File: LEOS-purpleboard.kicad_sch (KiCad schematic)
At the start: 5 parts, among them J3 Conn_01x07_Socket, J4 Conn_01x07_Socket, J5 Conn_01x06_Socket, J6 Conn_01x06_Socket, J7 Conn_01x04_Pin

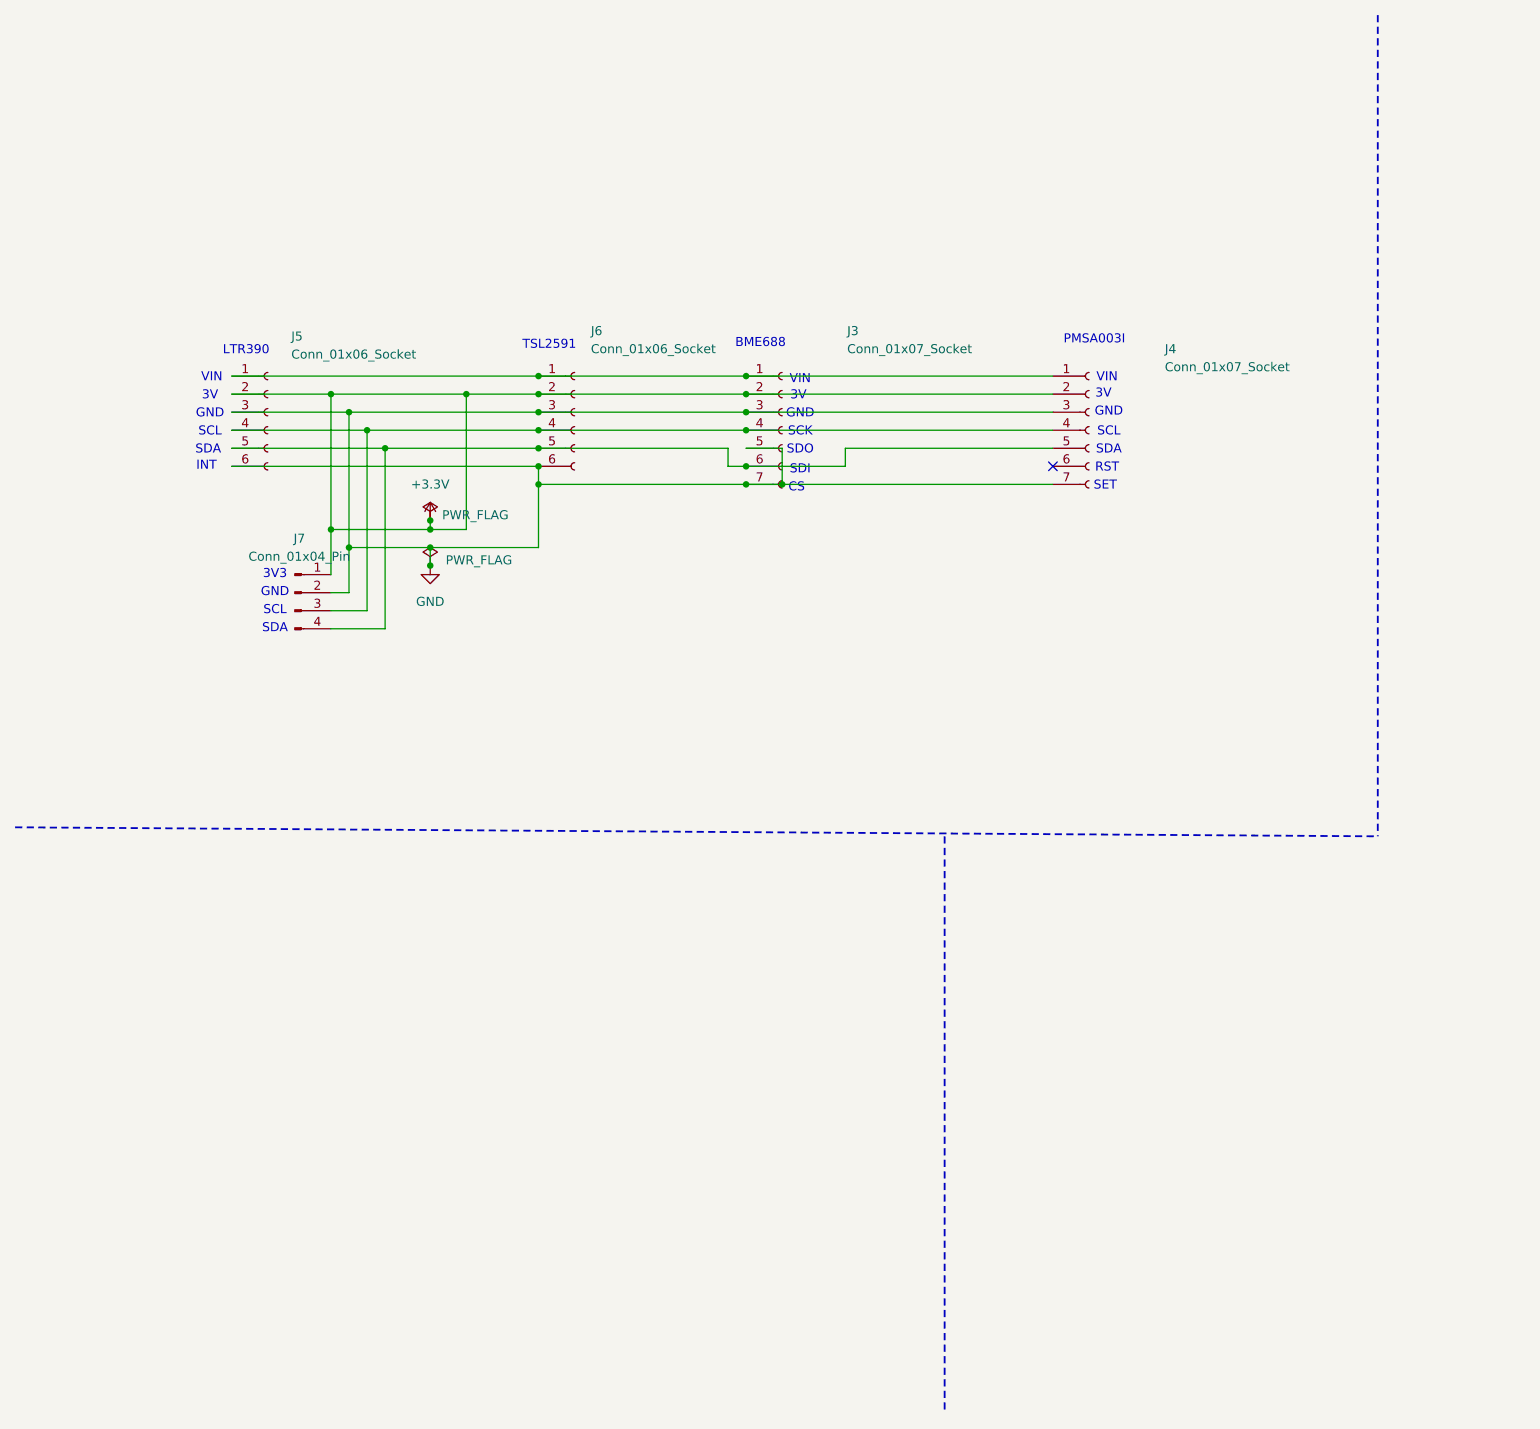
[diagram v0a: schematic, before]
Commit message: Fix flipped pinouts, update 3D model, and redesign schematic
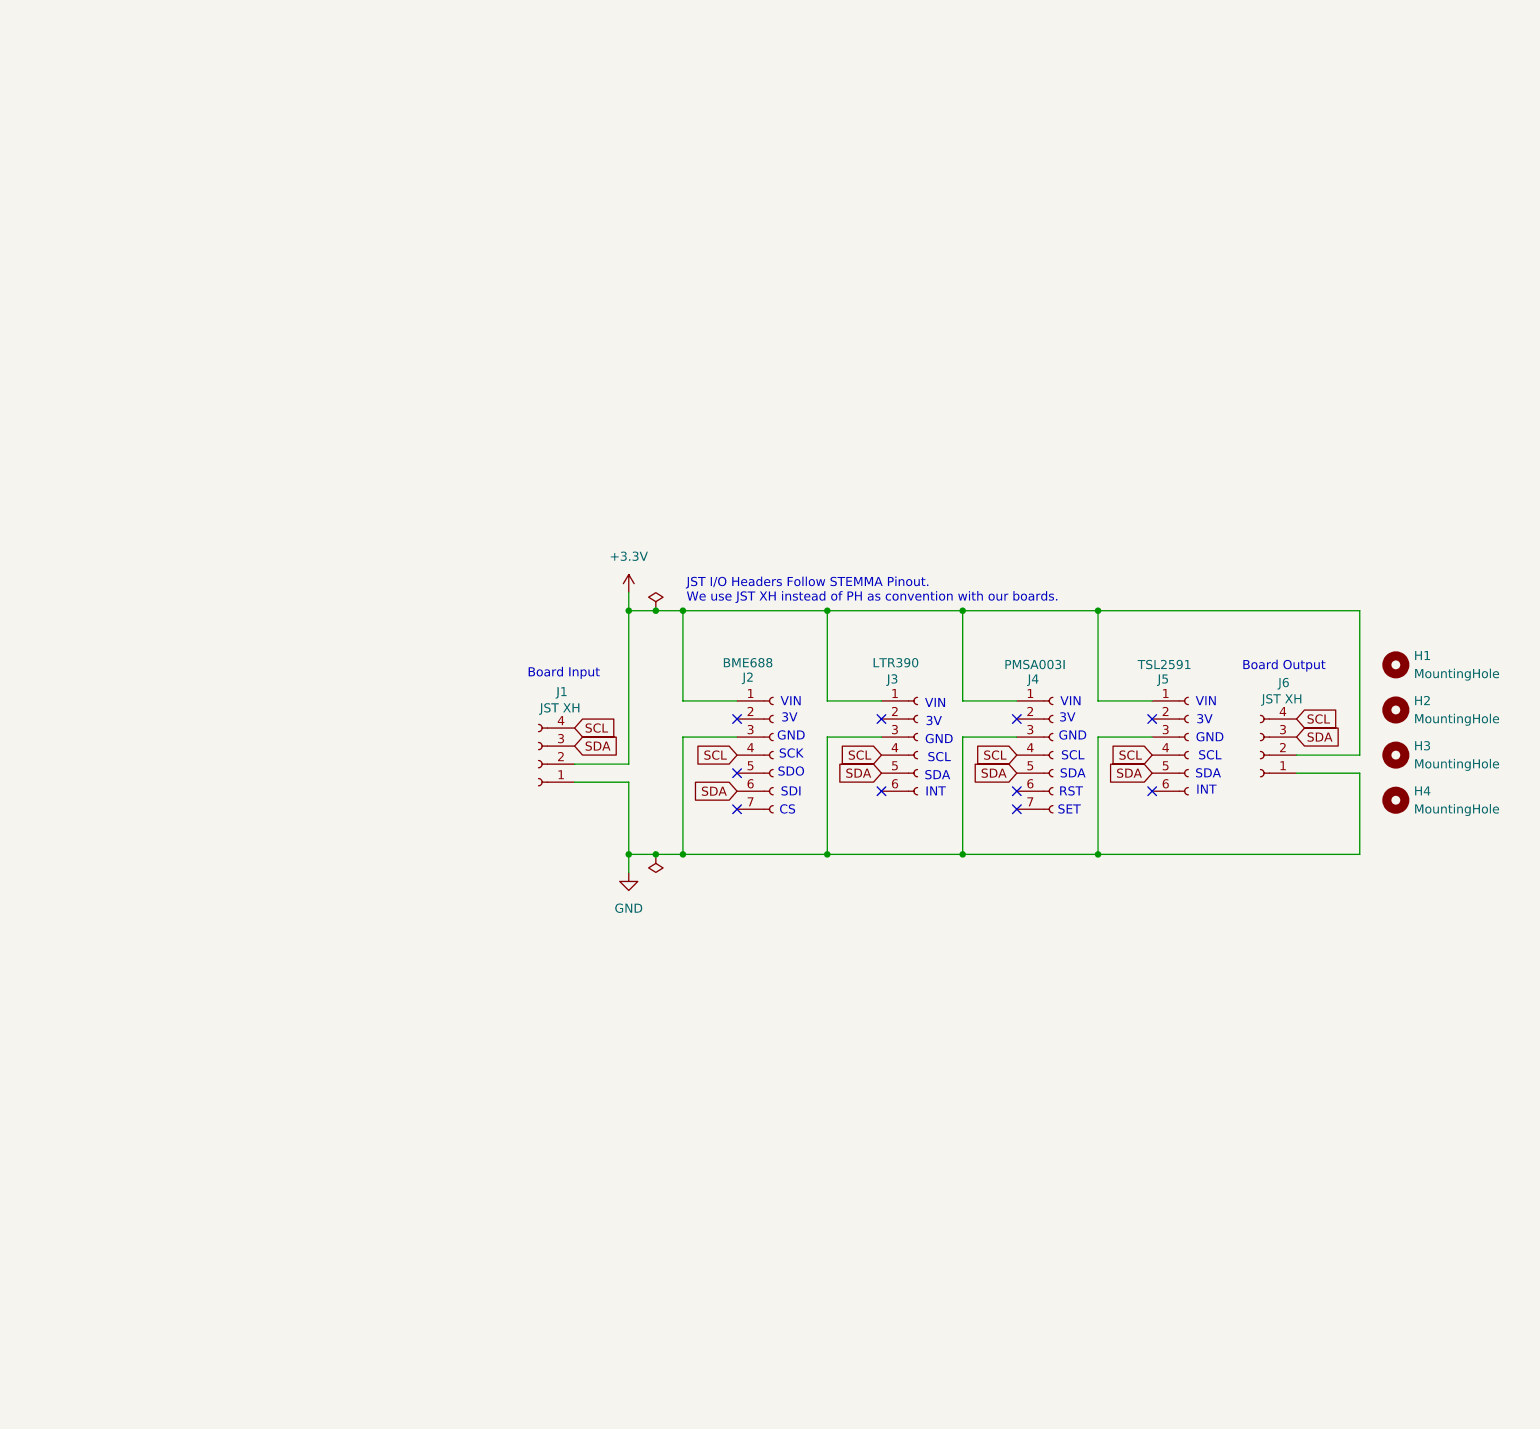
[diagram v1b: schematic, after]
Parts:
- removed J7: Conn_01x04_Pin, Connector_JST:JST_XH_S4B-XH-A_1x04_P2.50mm_Horizontal, symbol Connector:Conn_01x04_Pin
- added H1, H2, H3, H4: MountingHole, MountingHole:MountingHole_3.2mm_M3, symbol Mechanical:MountingHole
- added J1, J6: JST XH, Connector_JST:JST_XH_S4B-XH-A_1x04_P2.50mm_Horizontal, symbol Connector:Conn_01x04_Socket
- J2: renamed from J3; value Conn_01x07_Socket -> BME688; footprint Connector_JST:JST_XH_B7B-XH-A_1x07_P2.50mm_Vertical -> Connector_PinHeader_2.54mm:PinHeader_1x07_P2.54mm_Vertical
- J3: renamed from J5; value Conn_01x06_Socket -> LTR390; footprint Connector_JST:JST_XH_B6B-XH-A_1x06_P2.50mm_Vertical -> Connector_PinHeader_2.54mm:PinHeader_1x06_P2.54mm_Vertical
- J4: value Conn_01x07_Socket -> PMSA003I; footprint Connector_JST:JST_XH_B7B-XH-A_1x07_P2.50mm_Vertical -> Connector_PinHeader_2.54mm:PinHeader_1x07_P2.54mm_Vertical
- J5: renamed from J6; value Conn_01x06_Socket -> TSL2591; footprint Connector_JST:JST_XH_B6B-XH-A_1x06_P2.50mm_Vertical -> Connector_PinHeader_2.54mm:PinHeader_1x06_P2.54mm_Vertical
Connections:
- net +3.3V: now also J2.1 (Pin_1), J3.1 (Pin_1), J4.1 (Pin_1), J5.1 (Pin_1), J1.2 (Pin_2), J6.2 (Pin_2); no longer J2.2 (Pin_2), J3.2 (Pin_2), J4.2 (Pin_2), J5.2 (Pin_2)
- net GND: now also J1.1 (Pin_1), J6.1 (Pin_1); no longer J2.5 (Pin_5), J2.7 (Pin_7), J3.6 (Pin_6), J4.7 (Pin_7), J5.6 (Pin_6)
- net SCL: now reaches J2.4 (Pin_4), J3.4 (Pin_4), J4.4 (Pin_4), J5.4 (Pin_4)
- net SCL: now also J1.4 (Pin_4), J6.4 (Pin_4)
- net SDA: now reaches J2.6 (Pin_6), J3.5 (Pin_5), J4.5 (Pin_5), J5.5 (Pin_5)
- net SDA: now also J1.3 (Pin_3), J6.3 (Pin_3)
- no-connect marks 1 -> 10
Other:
- note added: "Board Input"
- note added: "Board Output"
- note added: "JST I/O Headers Follow STEMMA Pinout. We use JST XH instead of PH as convention with our boards."
- note removed: "3V3"
- note removed: "BME688"
- note removed: "LTR390"
- note removed: "PMSA003I"
- note removed: "TSL2591"
- title: LEOS Stack - Microcontroller & Connectivity -> LEOS Purpleboard
- moved on the sheet: J2, J3, J4, J5
